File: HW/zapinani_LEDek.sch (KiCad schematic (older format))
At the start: 4 parts, among them Q3 Q_PMOS_DGS, Q4 Q_PMOS_DGS

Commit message: repair project
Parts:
- renumbered R13 to R14, R14 to R15
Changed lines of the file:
@@
 P 2650 3800
 AR Path="/5F8EC656" Ref="R?"  Part="1"
-AR Path="/5F7BA54B/5F8EC656" Ref="R13"  Part="1"
+AR Path="/5F7BA54B/5F8EC656" Ref="R14"  Part="1"
 AR Path="/5F7BA54B/5F7BCB45/5F8EC656" Ref="R?"  Part="1"
 AR Path="/5F7BA54B/5F7BCBA6/5F8EC656" Ref="R?"  Part="1"
 AR Path="/5F7BA54B/5F7BCC0A/5F8EC656" Ref="R?"  Part="1"
 AR Path="/5F7BA54B/5F7BCC69/5F8EC656" Ref="R?"  Part="1"
-F 0 "R13" H 2720 3846 50  0000 L CNN
+F 0 "R14" H 2720 3846 50  0000 L CNN
 F 1 "10k" H 2720 3755 50  0000 L CNN
 F 2 "Resistor_SMD:R_0402_1005Metric" V 2580 3800 50  0001 C CNN
@@
 	0    1    -1   0
 $EndComp
-$Comp
-L Device:R R?
-U 1 1 5F8ECA6B
-P 5700 3800
-AR Path="/5F8ECA6B" Ref="R?"  Part="1"
-AR Path="/5F7BA54B/5F8ECA6B" Ref="R14"  Part="1"
-AR Path="/5F7BA54B/5F7BCB45/5F8ECA6B" Ref="R?"  Part="1"
-AR Path="/5F7BA54B/5F7BCBA6/5F8ECA6B" Ref="R?"  Part="1"
-AR Path="/5F7BA54B/5F7BCC0A/5F8ECA6B" Ref="R?"  Part="1"
-AR Path="/5F7BA54B/5F7BCC69/5F8ECA6B" Ref="R?"  Part="1"
-F 0 "R14" H 5770 3846 50  0000 L CNN
-F 1 "10k" H 5770 3755 50  0000 L CNN
-F 2 "Resistor_SMD:R_0402_1005Metric" V 5630 3800 50  0001 C CNN
-F 3 "~" H 5700 3800 50  0001 C CNN
-F 4 "C25744" H 5700 3800 50  0001 C CNN "LCSC"
-	1    5700 3800
-	1    0    0    -1
-$EndComp
 Wire Wire Line
 	5250 3200 5500 3200
@@
 Text Notes 6250 3150 0    50   ~ 0
 OUT\n
+$Comp
+L Device:R R?
+U 1 1 5F8ECA6B
+P 5700 3800
+AR Path="/5F8ECA6B" Ref="R?"  Part="1"
+AR Path="/5F7BA54B/5F8ECA6B" Ref="R15"  Part="1"
+AR Path="/5F7BA54B/5F7BCB45/5F8ECA6B" Ref="R?"  Part="1"
+AR Path="/5F7BA54B/5F7BCBA6/5F8ECA6B" Ref="R?"  Part="1"
+AR Path="/5F7BA54B/5F7BCC0A/5F8ECA6B" Ref="R?"  Part="1"
+AR Path="/5F7BA54B/5F7BCC69/5F8ECA6B" Ref="R?"  Part="1"
+F 0 "R15" H 5770 3846 50  0000 L CNN
+F 1 "10k" H 5770 3755 50  0000 L CNN
+F 2 "Resistor_SMD:R_0402_1005Metric" V 5630 3800 50  0001 C CNN
+F 3 "~" H 5700 3800 50  0001 C CNN
+F 4 "C25744" H 5700 3800 50  0001 C CNN "LCSC"
+	1    5700 3800
+	1    0    0    -1
+$EndComp
 $EndSCHEMATC

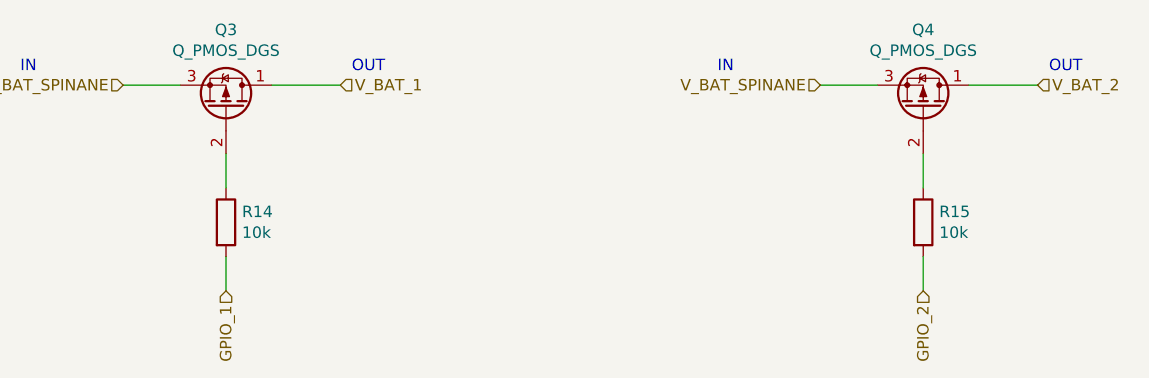
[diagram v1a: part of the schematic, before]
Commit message: repair some misakes from prototype
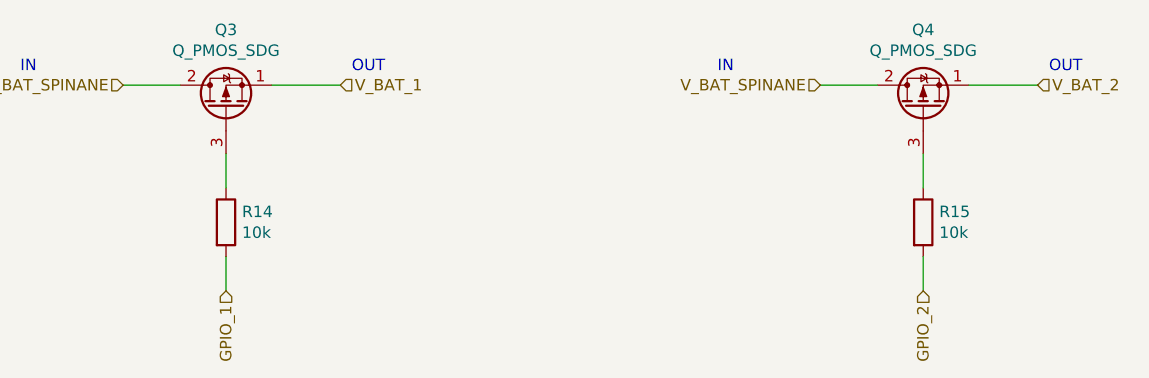
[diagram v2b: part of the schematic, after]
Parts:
- removed Q3, Q4: Q_PMOS_DGS, Package_TO_SOT_SMD:SOT-23, symbol Device:Q_PMOS_DGS
- added Q3, Q4: Q_PMOS_SDG, symbol Device:Q_PMOS_SDG
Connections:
- net V_BAT_1: now also Q3.1 (S)
- net V_BAT_2: now also Q4.1 (S)
- net V_BAT_SPINANE: now also Q3.2 (D), Q4.2 (D)
- net at R14.1: now also Q3.3 (G)
- net at R15.1: now also Q4.3 (G)
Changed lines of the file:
@@
 GPIO_1
-$Comp
-L Device:Q_PMOS_DGS Q?
-U 1 1 5F8EC64F
-P 2650 3300
-AR Path="/5F8EC64F" Ref="Q?"  Part="1"
-AR Path="/5F7BA54B/5F8EC64F" Ref="Q3"  Part="1"
-AR Path="/5F7BA54B/5F7BCB45/5F8EC64F" Ref="Q?"  Part="1"
-AR Path="/5F7BA54B/5F7BCBA6/5F8EC64F" Ref="Q?"  Part="1"
-AR Path="/5F7BA54B/5F7BCC0A/5F8EC64F" Ref="Q?"  Part="1"
-AR Path="/5F7BA54B/5F7BCC69/5F8EC64F" Ref="Q?"  Part="1"
-F 0 "Q3" V 2992 3300 50  0000 C CNN
-F 1 "Q_PMOS_DGS" V 2901 3300 50  0000 C CNN
-F 2 "Package_TO_SOT_SMD:SOT-23" H 2850 3400 50  0001 C CNN
-F 3 "~" H 2650 3300 50  0001 C CNN
-F 4 "C15127" H 2650 3300 50  0001 C CNN "LCSC"
-F 5 "0;0;180" H 2650 3300 50  0001 C CNN "JLCPCB_CORRECTION"
-	1    2650 3300
-	0    1    -1   0
-$EndComp
 $Comp
 L Device:R R?
@@
 Text HLabel 5700 4100 3    50   Input ~ 0
 GPIO_2
-$Comp
-L Device:Q_PMOS_DGS Q?
-U 1 1 5F8ECA64
-P 5700 3300
-AR Path="/5F8ECA64" Ref="Q?"  Part="1"
-AR Path="/5F7BA54B/5F8ECA64" Ref="Q4"  Part="1"
-AR Path="/5F7BA54B/5F7BCB45/5F8ECA64" Ref="Q?"  Part="1"
-AR Path="/5F7BA54B/5F7BCBA6/5F8ECA64" Ref="Q?"  Part="1"
-AR Path="/5F7BA54B/5F7BCC0A/5F8ECA64" Ref="Q?"  Part="1"
-AR Path="/5F7BA54B/5F7BCC69/5F8ECA64" Ref="Q?"  Part="1"
-F 0 "Q4" V 6042 3300 50  0000 C CNN
-F 1 "Q_PMOS_DGS" V 5951 3300 50  0000 C CNN
-F 2 "Package_TO_SOT_SMD:SOT-23" H 5900 3400 50  0001 C CNN
-F 3 "~" H 5700 3300 50  0001 C CNN
-F 4 "C15127" H 5700 3300 50  0001 C CNN "LCSC"
-F 5 "0;0;180" H 5700 3300 50  0001 C CNN "JLCPCB_CORRECTION"
-	1    5700 3300
-	0    1    -1   0
-$EndComp
 Wire Wire Line
 	5250 3200 5500 3200
@@
 	1    0    0    -1
 $EndComp
+$Comp
+L Device:Q_PMOS_SDG Q3
+U 1 1 5FAF79CC
+P 2650 3300
+F 0 "Q3" V 2992 3300 50  0000 C CNN
+F 1 "Q_PMOS_SDG" V 2901 3300 50  0000 C CNN
+F 2 "" H 2850 3400 50  0001 C CNN
+F 3 "~" H 2650 3300 50  0001 C CNN
+	1    2650 3300
+	0    -1   -1   0
+$EndComp
+$Comp
+L Device:Q_PMOS_SDG Q4
+U 1 1 5FAF7FFA
+P 5700 3300
+F 0 "Q4" V 6042 3300 50  0000 C CNN
+F 1 "Q_PMOS_SDG" V 5951 3300 50  0000 C CNN
+F 2 "" H 5900 3400 50  0001 C CNN
+F 3 "~" H 5700 3300 50  0001 C CNN
+	1    5700 3300
+	0    -1   -1   0
+$EndComp
 $EndSCHEMATC

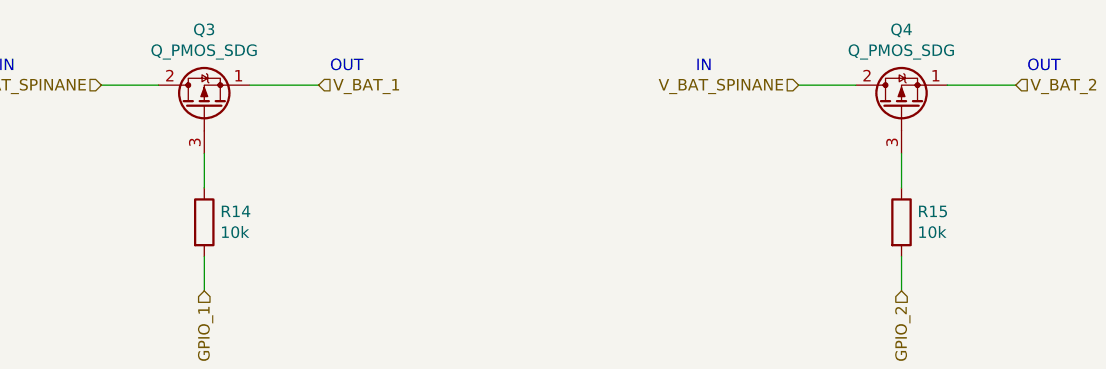
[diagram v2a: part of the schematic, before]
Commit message: repair mistake with tranzistors, repair programming ESP PICO
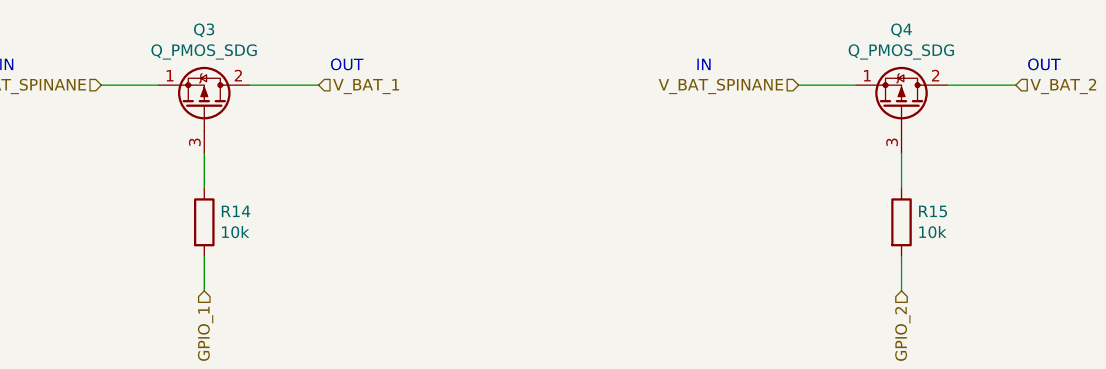
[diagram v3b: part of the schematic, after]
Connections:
- net V_BAT_1: now also Q3.2 (D); no longer Q3.1 (S)
- net V_BAT_2: now also Q4.2 (D); no longer Q4.1 (S)
- net V_BAT_SPINANE: now also Q3.1 (S), Q4.1 (S); no longer Q3.2 (D), Q4.2 (D)
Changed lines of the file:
@@
 F 3 "~" H 2650 3300 50  0001 C CNN
 	1    2650 3300
-	0    -1   -1   0
+	0    1    -1   0
 $EndComp
 $Comp
@@
 F 3 "~" H 5700 3300 50  0001 C CNN
 	1    5700 3300
-	0    -1   -1   0
+	0    1    -1   0
 $EndComp
 $EndSCHEMATC

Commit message: deposit of DPS, start v1.0
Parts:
- added Q? (x4): Q_NMOS_SDG, symbol Device:Q_NMOS_SDG
- added Q? (x2): Q_PMOS_SDG, symbol Device:Q_PMOS_SDG
- added R? (x4): 100k, Resistor_SMD:R_0402_1005Metric, symbol Device:R
- added R? (x2): 10k, Resistor_SMD:R_0402_1005Metric, symbol Device:R
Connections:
- net GPIO_1: now also Q?.3 (G), R?.1; no longer R14.2
- net GPIO_2: now also Q?.3 (G), R?.1; no longer R15.2
- net V_BAT_SPINANE: now also R14.1, R15.1, Q?.1 (S), Q?.1 (S), R?.1, R?.1
- net at Q3.3 (G): now also R14.2, Q?.2 (D); no longer R14.1
- net at Q4.3 (G): now also R15.2, Q?.2 (D); no longer R15.1
- new net: Q?.2 (D), Q?.3 (G), R?.2 (x2)
- new net GND: Q?.1 (S), Q?.1 (S), Q?.1 (S), Q?.1 (S), R?.2, R?.2, R?.2, R?.2
- new net GPIO_3: Q?.3 (G), R?.1
- new net GPIO_4: Q?.3 (G), R?.1
- new net V_BAT_3: Q?.2 (D)
- new net V_BAT_4: Q?.2 (D)
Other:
- moved on the sheet: R14, R15

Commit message: start place components
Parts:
- removed Q?: Q_PMOS_SDG, symbol Device:Q_PMOS_SDG
- removed Q?: Q_NMOS_SDG, symbol Device:Q_NMOS_SDG
- removed R?: 10k, Resistor_SMD:R_0402_1005Metric, symbol Device:R
- removed R?: 100k, Resistor_SMD:R_0402_1005Metric, symbol Device:R
- Q4, Q6, Q8, Q9: renamed from Q?; footprint (none) -> Package_TO_SOT_SMD:SOT-23
- Q5: renamed from Q3; footprint (none) -> Package_TO_SOT_SMD:SOT-23
- Q7: renamed from Q4; footprint (none) -> Package_TO_SOT_SMD:SOT-23
- gave numbers to parts that had none: 4
- renumbered R14 to R15, R15 to R17
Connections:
- net V_BAT_1 renamed V_LED_1
- net V_BAT_2 renamed V_LED_2
- net V_BAT_3 renamed V_LED_3
- net V_BAT_SPINANE renamed +5V

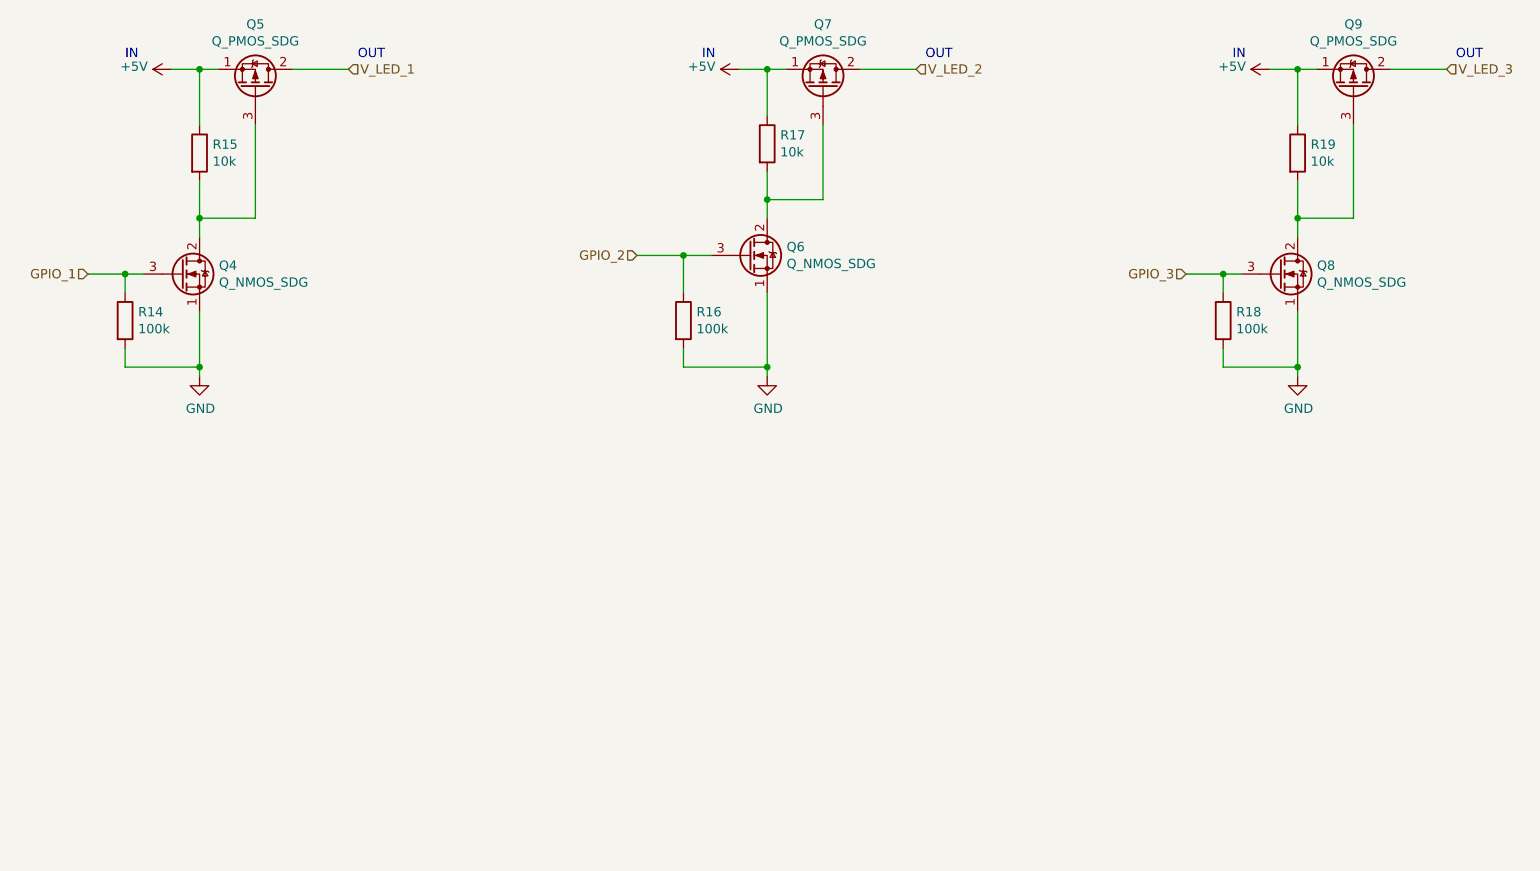
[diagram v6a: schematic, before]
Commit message: repair footprint of P and N MOS, add order codes for JLCPCB, preparing for fab
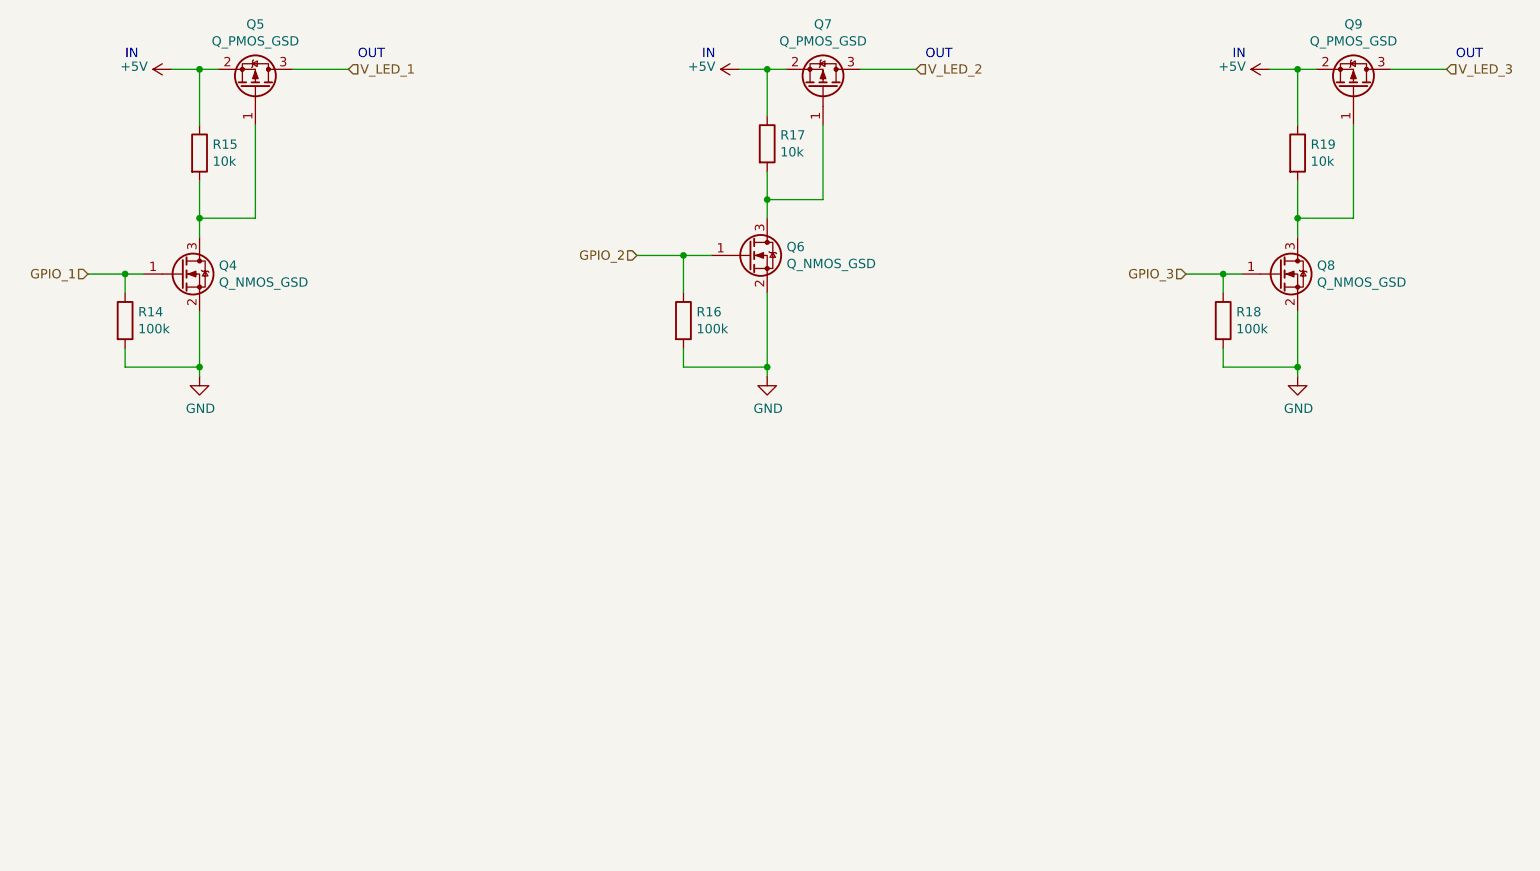
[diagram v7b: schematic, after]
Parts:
- removed Q4, Q6, Q8: Q_NMOS_SDG, Package_TO_SOT_SMD:SOT-23, symbol Device:Q_NMOS_SDG
- removed Q5, Q7, Q9: Q_PMOS_SDG, Package_TO_SOT_SMD:SOT-23, symbol Device:Q_PMOS_SDG
- added Q4, Q6, Q8: Q_NMOS_GSD, Package_TO_SOT_SMD:SOT-23, symbol Device:Q_NMOS_GSD
- added Q5, Q7, Q9: Q_PMOS_GSD, Package_TO_SOT_SMD:SOT-23, symbol Device:Q_PMOS_GSD
- R14, R16, R18: JLCPCB_CORRECTION (none) -> 0;0;0; LCSC (none) -> C25741
- R15, R17, R19: JLCPCB_CORRECTION (none) -> 0;0;0
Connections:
- net +5V: now also Q5.2 (S), Q7.2 (S), Q9.2 (S)
- net GND: now also Q4.2 (S), Q6.2 (S), Q8.2 (S)
- net GPIO_1: now also Q4.1 (G)
- net GPIO_2: now also Q6.1 (G)
- net GPIO_3: now also Q8.1 (G)
- net V_LED_1: now also Q5.3 (D)
- net V_LED_2: now also Q7.3 (D)
- net V_LED_3: now also Q9.3 (D)
- net at R15.2: now also Q4.3 (D), Q5.1 (G)
- net at R17.2: now also Q6.3 (D), Q7.1 (G)
- net at R19.2: now also Q8.3 (D), Q9.1 (G)
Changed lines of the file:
@@
 F 3 "~" H 2350 3650 50  0001 C CNN
 F 4 "C25744" H 2350 3650 50  0001 C CNN "LCSC"
+F 5 "0;0;0" H 2350 3650 50  0001 C CNN "JLCPCB_CORRECTION"
 	1    2350 3650
 	1    0    0    -1
@@
 F 3 "~" H 5400 3600 50  0001 C CNN
 F 4 "C25744" H 5400 3600 50  0001 C CNN "LCSC"
+F 5 "0;0;0" H 5400 3600 50  0001 C CNN "JLCPCB_CORRECTION"
 	1    5400 3600
 	1    0    0    -1
-$EndComp
-$Comp
-L Device:Q_PMOS_SDG Q5
-U 1 1 5FAF79CC
-P 2650 3300
-F 0 "Q5" V 2992 3300 50  0000 C CNN
-F 1 "Q_PMOS_SDG" V 2901 3300 50  0000 C CNN
-F 2 "Package_TO_SOT_SMD:SOT-23" H 2850 3400 50  0001 C CNN
-F 3 "~" H 2650 3300 50  0001 C CNN
-	1    2650 3300
-	0    1    -1   0
-$EndComp
-$Comp
-L Device:Q_PMOS_SDG Q7
-U 1 1 5FAF7FFA
-P 5700 3300
-F 0 "Q7" V 6042 3300 50  0000 C CNN
-F 1 "Q_PMOS_SDG" V 5951 3300 50  0000 C CNN
-F 2 "Package_TO_SOT_SMD:SOT-23" H 5900 3400 50  0001 C CNN
-F 3 "~" H 5700 3300 50  0001 C CNN
-	1    5700 3300
-	0    1    -1   0
 $EndComp
 Wire Wire Line
@@
 Wire Wire Line
 	2350 3200 2450 3200
-$Comp
-L Device:Q_NMOS_SDG Q4
-U 1 1 5FB7294B
-P 2250 4300
-F 0 "Q4" H 2454 4346 50  0000 L CNN
-F 1 "Q_NMOS_SDG" H 2454 4255 50  0000 L CNN
-F 2 "Package_TO_SOT_SMD:SOT-23" H 2450 4400 50  0001 C CNN
-F 3 "~" H 2250 4300 50  0001 C CNN
-	1    2250 4300
-	1    0    0    -1
-$EndComp
 $Comp
 L power:GND #PWR0132
@@
 F 2 "Resistor_SMD:R_0402_1005Metric" V 1880 4550 50  0001 C CNN
 F 3 "~" H 1950 4550 50  0001 C CNN
-F 4 "" H 1950 4550 50  0001 C CNN "LCSC"
+F 4 "C25741" H 1950 4550 50  0001 C CNN "LCSC"
+F 5 "0;0;0" H 1950 4550 50  0001 C CNN "JLCPCB_CORRECTION"
 	1    1950 4550
 	1    0    0    -1
@@
 Wire Wire Line
 	5400 3200 5500 3200
-$Comp
-L Device:Q_NMOS_SDG Q6
-U 1 1 5FB74924
-P 5300 4200
-F 0 "Q6" H 5504 4246 50  0000 L CNN
-F 1 "Q_NMOS_SDG" H 5504 4155 50  0000 L CNN
-F 2 "Package_TO_SOT_SMD:SOT-23" H 5500 4300 50  0001 C CNN
-F 3 "~" H 5300 4200 50  0001 C CNN
-	1    5300 4200
-	1    0    0    -1
-$EndComp
 $Comp
 L Device:R R?
@@
 F 2 "Resistor_SMD:R_0402_1005Metric" V 4880 4550 50  0001 C CNN
 F 3 "~" H 4950 4550 50  0001 C CNN
-F 4 "" H 4950 4550 50  0001 C CNN "LCSC"
+F 4 "C25741" H 4950 4550 50  0001 C CNN "LCSC"
+F 5 "0;0;0" H 4950 4550 50  0001 C CNN "JLCPCB_CORRECTION"
 	1    4950 4550
 	1    0    0    -1
@@
 F 3 "~" H 8250 3650 50  0001 C CNN
 F 4 "C25744" H 8250 3650 50  0001 C CNN "LCSC"
+F 5 "0;0;0" H 8250 3650 50  0001 C CNN "JLCPCB_CORRECTION"
 	1    8250 3650
 	1    0    0    -1
@@
 Text Notes 9100 3150 0    50   ~ 0
 OUT\n
-$Comp
-L Device:Q_PMOS_SDG Q9
-U 1 1 5FB8D0BA
-P 8550 3300
-F 0 "Q9" V 8892 3300 50  0000 C CNN
-F 1 "Q_PMOS_SDG" V 8801 3300 50  0000 C CNN
-F 2 "Package_TO_SOT_SMD:SOT-23" H 8750 3400 50  0001 C CNN
-F 3 "~" H 8550 3300 50  0001 C CNN
-	1    8550 3300
-	0    1    -1   0
-$EndComp
 Wire Wire Line
 	8550 4000 8250 4000
@@
 Wire Wire Line
 	8250 3200 8350 3200
-$Comp
-L Device:Q_NMOS_SDG Q8
-U 1 1 5FB8D0C6
-P 8150 4300
-F 0 "Q8" H 8354 4346 50  0000 L CNN
-F 1 "Q_NMOS_SDG" H 8354 4255 50  0000 L CNN
-F 2 "Package_TO_SOT_SMD:SOT-23" H 8350 4400 50  0001 C CNN
-F 3 "~" H 8150 4300 50  0001 C CNN
-	1    8150 4300
-	1    0    0    -1
-$EndComp
 $Comp
 L power:GND #PWR0134
@@
 F 2 "Resistor_SMD:R_0402_1005Metric" V 7780 4550 50  0001 C CNN
 F 3 "~" H 7850 4550 50  0001 C CNN
-F 4 "" H 7850 4550 50  0001 C CNN "LCSC"
+F 4 "C25741" H 7850 4550 50  0001 C CNN "LCSC"
+F 5 "0;0;0" H 7850 4550 50  0001 C CNN "JLCPCB_CORRECTION"
 	1    7850 4550
 	1    0    0    -1
@@
 	0    -1   -1   0
 $EndComp
+$Comp
+L Device:Q_PMOS_GSD Q5
+U 1 1 5FC5A38E
+P 2650 3300
+F 0 "Q5" V 2992 3300 50  0000 C CNN
+F 1 "Q_PMOS_GSD" V 2901 3300 50  0000 C CNN
+F 2 "Package_TO_SOT_SMD:SOT-23" H 2850 3400 50  0001 C CNN
+F 3 "~" H 2650 3300 50  0001 C CNN
+F 4 "C8492" H 2650 3300 50  0001 C CNN "LCSC"
+F 5 "0;0;180" H 2650 3300 50  0001 C CNN "JLCPCB_CORRECTION"
+	1    2650 3300
+	0    1    -1   0
+$EndComp
+$Comp
+L Device:Q_PMOS_GSD Q7
+U 1 1 5FC5B95E
+P 5700 3300
+F 0 "Q7" V 6042 3300 50  0000 C CNN
+F 1 "Q_PMOS_GSD" V 5951 3300 50  0000 C CNN
+F 2 "Package_TO_SOT_SMD:SOT-23" H 5900 3400 50  0001 C CNN
+F 3 "~" H 5700 3300 50  0001 C CNN
+F 4 "C8492" H 5700 3300 50  0001 C CNN "LCSC"
+F 5 "0;0;180" H 5700 3300 50  0001 C CNN "JLCPCB_CORRECTION"
+	1    5700 3300
+	0    1    -1   0
+$EndComp
+$Comp
+L Device:Q_PMOS_GSD Q9
+U 1 1 5FC5BC18
+P 8550 3300
+F 0 "Q9" V 8892 3300 50  0000 C CNN
+F 1 "Q_PMOS_GSD" V 8801 3300 50  0000 C CNN
+F 2 "Package_TO_SOT_SMD:SOT-23" H 8750 3400 50  0001 C CNN
+F 3 "~" H 8550 3300 50  0001 C CNN
+F 4 "C8492" H 8550 3300 50  0001 C CNN "LCSC"
+F 5 "0;0;180" H 8550 3300 50  0001 C CNN "JLCPCB_CORRECTION"
+	1    8550 3300
+	0    1    -1   0
+$EndComp
+$Comp
+L Device:Q_NMOS_GSD Q4
+U 1 1 5FC5C56E
+P 2250 4300
+F 0 "Q4" H 2454 4346 50  0000 L CNN
+F 1 "Q_NMOS_GSD" H 2454 4255 50  0000 L CNN
+F 2 "Package_TO_SOT_SMD:SOT-23" H 2450 4400 50  0001 C CNN
+F 3 "~" H 2250 4300 50  0001 C CNN
+F 4 "C8545" H 2250 4300 50  0001 C CNN "LCSC"
+F 5 "0;0;180" H 2250 4300 50  0001 C CNN "JLCPCB_CORRECTION"
+	1    2250 4300
+	1    0    0    -1
+$EndComp
+$Comp
+L Device:Q_NMOS_GSD Q6
+U 1 1 5FC5C97E
+P 5300 4200
+F 0 "Q6" H 5504 4246 50  0000 L CNN
+F 1 "Q_NMOS_GSD" H 5504 4155 50  0000 L CNN
+F 2 "Package_TO_SOT_SMD:SOT-23" H 5500 4300 50  0001 C CNN
+F 3 "~" H 5300 4200 50  0001 C CNN
+F 4 "C8545" H 5300 4200 50  0001 C CNN "LCSC"
+F 5 "0;0;180" H 5300 4200 50  0001 C CNN "JLCPCB_CORRECTION"
+	1    5300 4200
+	1    0    0    -1
+$EndComp
+$Comp
+L Device:Q_NMOS_GSD Q8
+U 1 1 5FC5CB0D
+P 8150 4300
+F 0 "Q8" H 8354 4346 50  0000 L CNN
+F 1 "Q_NMOS_GSD" H 8354 4255 50  0000 L CNN
+F 2 "Package_TO_SOT_SMD:SOT-23" H 8350 4400 50  0001 C CNN
+F 3 "~" H 8150 4300 50  0001 C CNN
+F 4 "C8545" H 8150 4300 50  0001 C CNN "LCSC"
+F 5 "0;0;180" H 8150 4300 50  0001 C CNN "JLCPCB_CORRECTION"
+	1    8150 4300
+	1    0    0    -1
+$EndComp
 $EndSCHEMATC
